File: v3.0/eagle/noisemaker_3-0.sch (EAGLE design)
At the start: 57 parts, among them IC1 REG1117

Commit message: board layout, all text complete. ready for manufacture, RC1
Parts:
- removed U$3: OSHW-LOGOS, SparkFun:OSHW-LOGOS
- added LOGO1: OSHW-LOGOM, SparkFun-Aesthetics:OSHW-LOGOM
- renumbered JP5 to ICSP, LED7 to LED1, LED8 to LED2, POWER to PWR
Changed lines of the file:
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@@
 <part name="JP7" library="SparkFun" deviceset="M12" device="PTH" value=""/>
 <part name="GND4" library="SparkFun" deviceset="GND" device=""/>
-<part name="U$3" library="SparkFun" deviceset="OSHW-LOGO" device="S"/>
 <part name="ATMEGA32U4" library="SparkFun-DigitalIC" deviceset="ATMEGA32U4" device="TQFP" value="ATMEGA32U4"/>
 <part name="XTAL" library="SparkFun" deviceset="CRYSTAL" device="5X3" value="16MHz"/>
@@
 <part name="GND8" library="SparkFun" deviceset="GND" device=""/>
 <part name="GND10" library="SparkFun" deviceset="GND" device=""/>
-<part name="POWER" library="adafruit" deviceset="LED" device="CHIPLED_1206" value="Red"/>
+<part name="PWR" library="adafruit" deviceset="LED" device="CHIPLED_1206" value="Red"/>
 <part name="R1" library="SparkFun-Passives" deviceset="RESISTOR" device="1206" value="1K"/>
 <part name="GND11" library="SparkFun" deviceset="GND" device=""/>
@@
 <part name="P+6" library="SparkFun" deviceset="3.3V" device="" value="VCC"/>
 <part name="P+7" library="SparkFun" deviceset="3.3V" device="" value="VCC"/>
-<part name="JP5" library="SparkFun" deviceset="AVR_SPI_PRG_6" device="PTH" value="AVR_SPI"/>
+<part name="ICSP" library="SparkFun" deviceset="AVR_SPI_PRG_6" device="PTH" value="AVR_SPI"/>
 <part name="GND1" library="SparkFun" deviceset="GND" device=""/>
 <part name="P+9" library="SparkFun" deviceset="3.3V" device="" value="VCC"/>
@@
 <part name="R13" library="SparkFun-Passives" deviceset="RESISTOR" device="1206" value="1k"/>
 <part name="GND19" library="SparkFun" deviceset="GND" device=""/>
-<part name="LED7" library="adafruit" deviceset="LED" device="3MM"/>
-<part name="LED8" library="adafruit" deviceset="LED" device="3MM"/>
+<part name="LED1" library="adafruit" deviceset="LED" device="3MM"/>
+<part name="LED2" library="adafruit" deviceset="LED" device="3MM"/>
 <part name="GND17" library="supply1" deviceset="GND" device=""/>
 <part name="R14" library="SparkFun-Passives" deviceset="RESISTOR" device="1206"/>
@@
 <part name="NEOPIXEL" library="SparkFun-Connectors" deviceset="M03" device="LONGPADS"/>
 <part name="P+8" library="SparkFun" deviceset="3.3V" device="" value="VCC"/>
+<part name="LOGO1" library="SparkFun-Aesthetics" deviceset="OSHW-LOGO" device="M" value="OSHW-LOGOM"/>
 </parts>
 <sheets>
@@
 <instance part="JP7" gate="G$1" x="60.96" y="101.6"/>
 <instance part="GND4" gate="1" x="139.7" y="109.22" rot="R270"/>
-<instance part="U$3" gate="G$1" x="243.84" y="175.26"/>
 <instance part="ATMEGA32U4" gate="G$1" x="180.34" y="121.92" smashed="yes">
 <attribute name="NAME" x="166.37" y="161.036" size="1.778" layer="95"/>
@@
 <instance part="GND8" gate="1" x="33.02" y="137.16"/>
 <instance part="GND10" gate="1" x="99.06" y="137.16"/>
-<instance part="POWER" gate="G$1" x="99.06" y="147.32"/>
+<instance part="PWR" gate="G$1" x="99.06" y="147.32"/>
 <instance part="R1" gate="G$1" x="99.06" y="154.94" rot="R90"/>
 <instance part="GND11" gate="1" x="76.2" y="137.16"/>
@@
 <attribute name="VALUE" x="297.942" y="91.186" size="1.778" layer="96" rot="R270"/>
 </instance>
-<instance part="JP5" gate="G$1" x="167.64" y="55.88"/>
+<instance part="ICSP" gate="G$1" x="167.64" y="55.88"/>
 <instance part="GND1" gate="1" x="180.34" y="48.26"/>
 <instance part="P+9" gate="G$1" x="180.34" y="60.96" smashed="yes">
@@
 <instance part="R13" gate="G$1" x="251.46" y="18.796"/>
 <instance part="GND19" gate="1" x="261.62" y="18.796" rot="R90"/>
-<instance part="LED7" gate="G$1" x="162.56" y="23.876" rot="R180"/>
-<instance part="LED8" gate="G$1" x="162.56" y="13.716" rot="R180"/>
+<instance part="LED1" gate="G$1" x="162.56" y="23.876" rot="R180"/>
+<instance part="LED2" gate="G$1" x="162.56" y="13.716" rot="R180"/>
 <instance part="GND17" gate="1" x="177.8" y="30.48" rot="R90"/>
 <instance part="R14" gate="G$1" x="167.64" y="9.652" rot="R180"/>
@@
 <attribute name="VALUE" x="105.918" y="86.614" size="1.778" layer="96" rot="R90"/>
 </instance>
+<instance part="LOGO1" gate="G$1" x="292.1" y="35.56"/>
 </instances>
 <busses>
@@
 <segment>
 <pinref part="GND10" gate="1" pin="GND"/>
-<pinref part="POWER" gate="G$1" pin="C"/>
+<pinref part="PWR" gate="G$1" pin="C"/>
 <wire x1="99.06" y1="142.24" x2="99.06" y2="139.7" width="0.1524" layer="91"/>
 </segment>
@@
 <wire x1="177.8" y1="53.34" x2="180.34" y2="53.34" width="0.1524" layer="91"/>
 <wire x1="180.34" y1="53.34" x2="180.34" y2="50.8" width="0.1524" layer="91"/>
-<pinref part="JP5" gate="G$1" pin="6"/>
+<pinref part="ICSP" gate="G$1" pin="6"/>
 <pinref part="GND1" gate="1" pin="GND"/>
 </segment>
@@
 <wire x1="160.02" y1="53.34" x2="147.32" y2="53.34" width="0.1524" layer="91"/>
 <label x="147.32" y="53.34" size="1.778" layer="95"/>
-<pinref part="JP5" gate="G$1" pin="5"/>
+<pinref part="ICSP" gate="G$1" pin="5"/>
 </segment>
 </net>
@@
 <wire x1="160.02" y1="55.88" x2="147.32" y2="55.88" width="0.1524" layer="91"/>
 <label x="147.32" y="55.88" size="1.778" layer="95"/>
-<pinref part="JP5" gate="G$1" pin="3"/>
+<pinref part="ICSP" gate="G$1" pin="3"/>
 </segment>
 </net>
@@
 <wire x1="160.02" y1="58.42" x2="147.32" y2="58.42" width="0.1524" layer="91"/>
 <label x="147.32" y="58.42" size="1.778" layer="95"/>
-<pinref part="JP5" gate="G$1" pin="1"/>
+<pinref part="ICSP" gate="G$1" pin="1"/>
 </segment>
 </net>
@@
 <wire x1="177.8" y1="55.88" x2="187.96" y2="55.88" width="0.1524" layer="91"/>
 <label x="182.88" y="55.88" size="1.778" layer="95"/>
-<pinref part="JP5" gate="G$1" pin="4"/>
+<pinref part="ICSP" gate="G$1" pin="4"/>
 </segment>
 </net>
@@
 <wire x1="177.8" y1="58.42" x2="180.34" y2="58.42" width="0.1524" layer="91"/>
 <wire x1="180.34" y1="60.96" x2="180.34" y2="58.42" width="0.1524" layer="91"/>
-<pinref part="JP5" gate="G$1" pin="2"/>
+<pinref part="ICSP" gate="G$1" pin="2"/>
 <pinref part="P+9" gate="G$1" pin="3.3V"/>
 </segment>
@@
 </segment>
 <segment>
-<pinref part="LED7" gate="G$1" pin="A"/>
-<pinref part="LED8" gate="G$1" pin="C"/>
+<pinref part="LED1" gate="G$1" pin="A"/>
+<pinref part="LED2" gate="G$1" pin="C"/>
 <wire x1="162.56" y1="18.796" x2="162.56" y2="20.32" width="0.1524" layer="91"/>
 <wire x1="162.56" y1="20.32" x2="162.56" y2="21.336" width="0.1524" layer="91"/>
@@
 <net name="N$10" class="0">
 <segment>
-<pinref part="POWER" gate="G$1" pin="A"/>
+<pinref part="PWR" gate="G$1" pin="A"/>
 <pinref part="R1" gate="G$1" pin="1"/>
 </segment>
@@
 <segment>
 <pinref part="R18" gate="G$1" pin="1"/>
-<pinref part="LED7" gate="G$1" pin="C"/>
+<pinref part="LED1" gate="G$1" pin="C"/>
 <wire x1="162.56" y1="30.48" x2="162.56" y2="28.956" width="0.1524" layer="91"/>
 </segment>
@@
 <net name="N$13" class="0">
 <segment>
-<pinref part="LED8" gate="G$1" pin="A"/>
+<pinref part="LED2" gate="G$1" pin="A"/>
 <wire x1="162.56" y1="11.176" x2="162.56" y2="9.652" width="0.1524" layer="91"/>
 <pinref part="R14" gate="G$1" pin="2"/>

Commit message: small adjustments, this is final board
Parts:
- R14, R18: value (none) -> 330
- R15, R19: value (none) -> 10k
- R3, R8: value (none) -> 1M
- R9: value (none) -> 22k
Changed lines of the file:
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@@
 <part name="C11" library="SparkFun-Capacitors" deviceset="CAP" device="1206" value="0.1uF"/>
 <part name="P+5" library="SparkFun" deviceset="3.3V" device="" value="VCC"/>
-<part name="R3" library="SparkFun-Passives" deviceset="RESISTOR" device="1206"/>
-<part name="R8" library="SparkFun-Passives" deviceset="RESISTOR" device="1206"/>
-<part name="R9" library="SparkFun-Passives" deviceset="RESISTOR" device="1206"/>
+<part name="R3" library="SparkFun-Passives" deviceset="RESISTOR" device="1206" value="1M"/>
+<part name="R8" library="SparkFun-Passives" deviceset="RESISTOR" device="1206" value="1M"/>
+<part name="R9" library="SparkFun-Passives" deviceset="RESISTOR" device="1206" value="22k"/>
 <part name="NPN" library="SparkFun-DiscreteSemi" deviceset="TRANSISTOR_NPN" device="SOT23-3"/>
 <part name="GND16" library="supply1" deviceset="GND" device=""/>
@@
 <part name="JP4" library="SparkFun-Connectors" deviceset="M01" device="PTH"/>
 <part name="SENSOR1" library="photo-elements" deviceset="M9960_11" device="" technology="B"/>
-<part name="R15" library="SparkFun-Passives" deviceset="RESISTOR" device="1206"/>
-<part name="R19" library="SparkFun-Passives" deviceset="RESISTOR" device="1206"/>
+<part name="R15" library="SparkFun-Passives" deviceset="RESISTOR" device="1206" value="10k"/>
+<part name="R19" library="SparkFun-Passives" deviceset="RESISTOR" device="1206" value="10k"/>
 <part name="SENSOR2" library="photo-elements" deviceset="M9960_11" device="" technology="B"/>
 <part name="GND21" library="supply1" deviceset="GND" device=""/>
@@
 <part name="LED2" library="adafruit" deviceset="LED" device="3MM"/>
 <part name="GND17" library="supply1" deviceset="GND" device=""/>
-<part name="R14" library="SparkFun-Passives" deviceset="RESISTOR" device="1206"/>
-<part name="R18" library="SparkFun-Passives" deviceset="RESISTOR" device="1206"/>
+<part name="R14" library="SparkFun-Passives" deviceset="RESISTOR" device="1206" value="330"/>
+<part name="R18" library="SparkFun-Passives" deviceset="RESISTOR" device="1206" value="330"/>
 <part name="POLE3" library="SparkFun-Connectors" deviceset="M01" device="PTH_LONGPAD"/>
 <part name="P+13" library="SparkFun" deviceset="3.3V" device="" value="VCC"/>

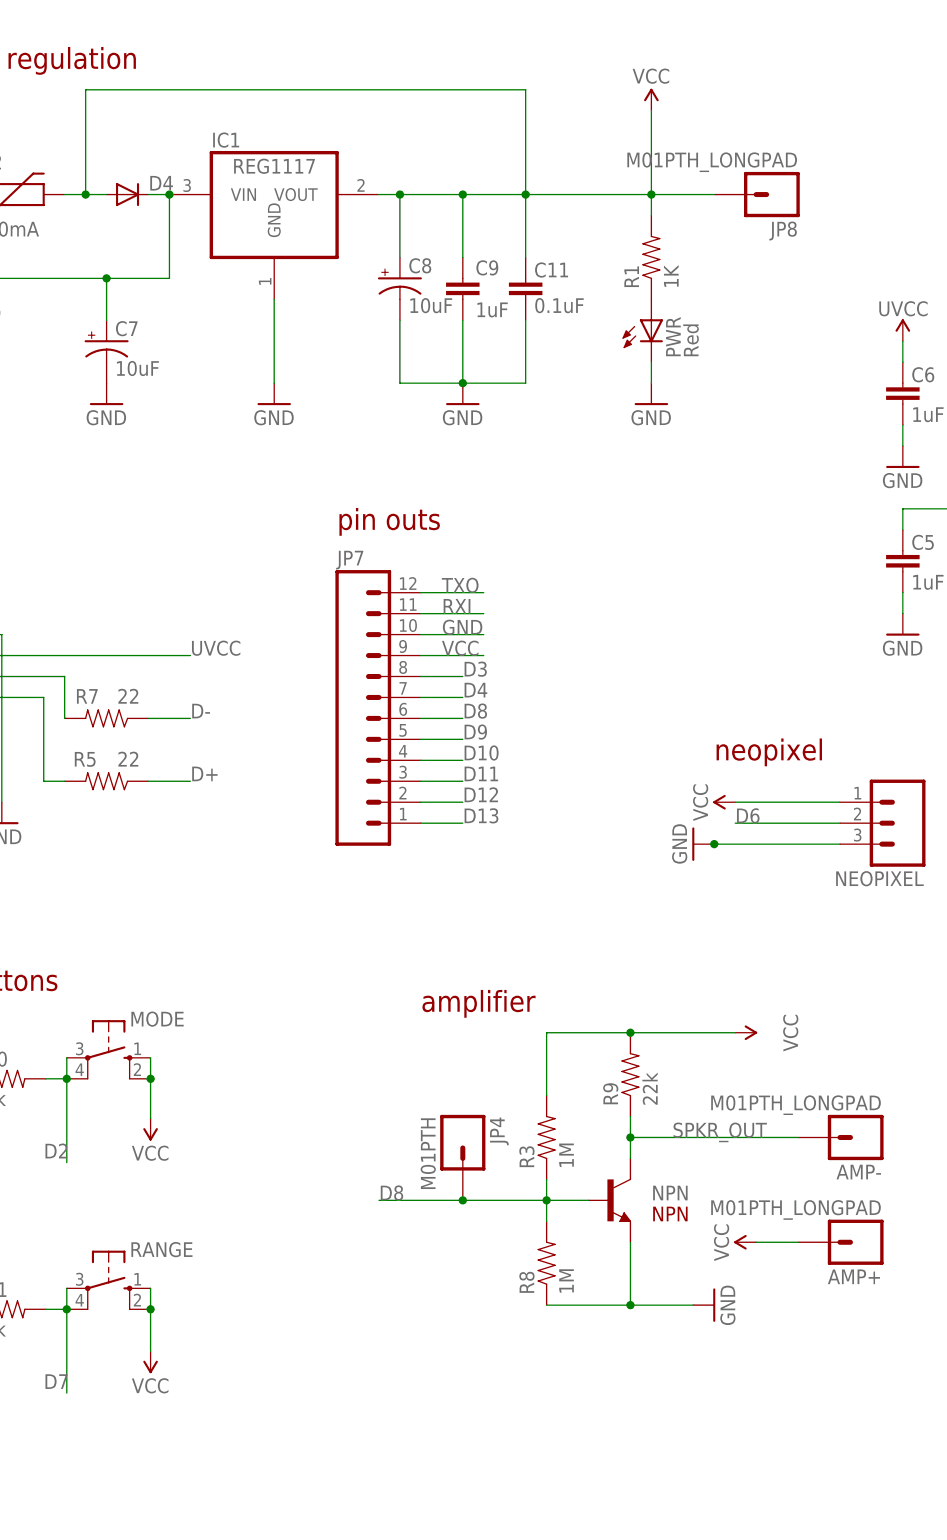
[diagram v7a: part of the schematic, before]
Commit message: updated voltage regulator, added second footprint for NPN options
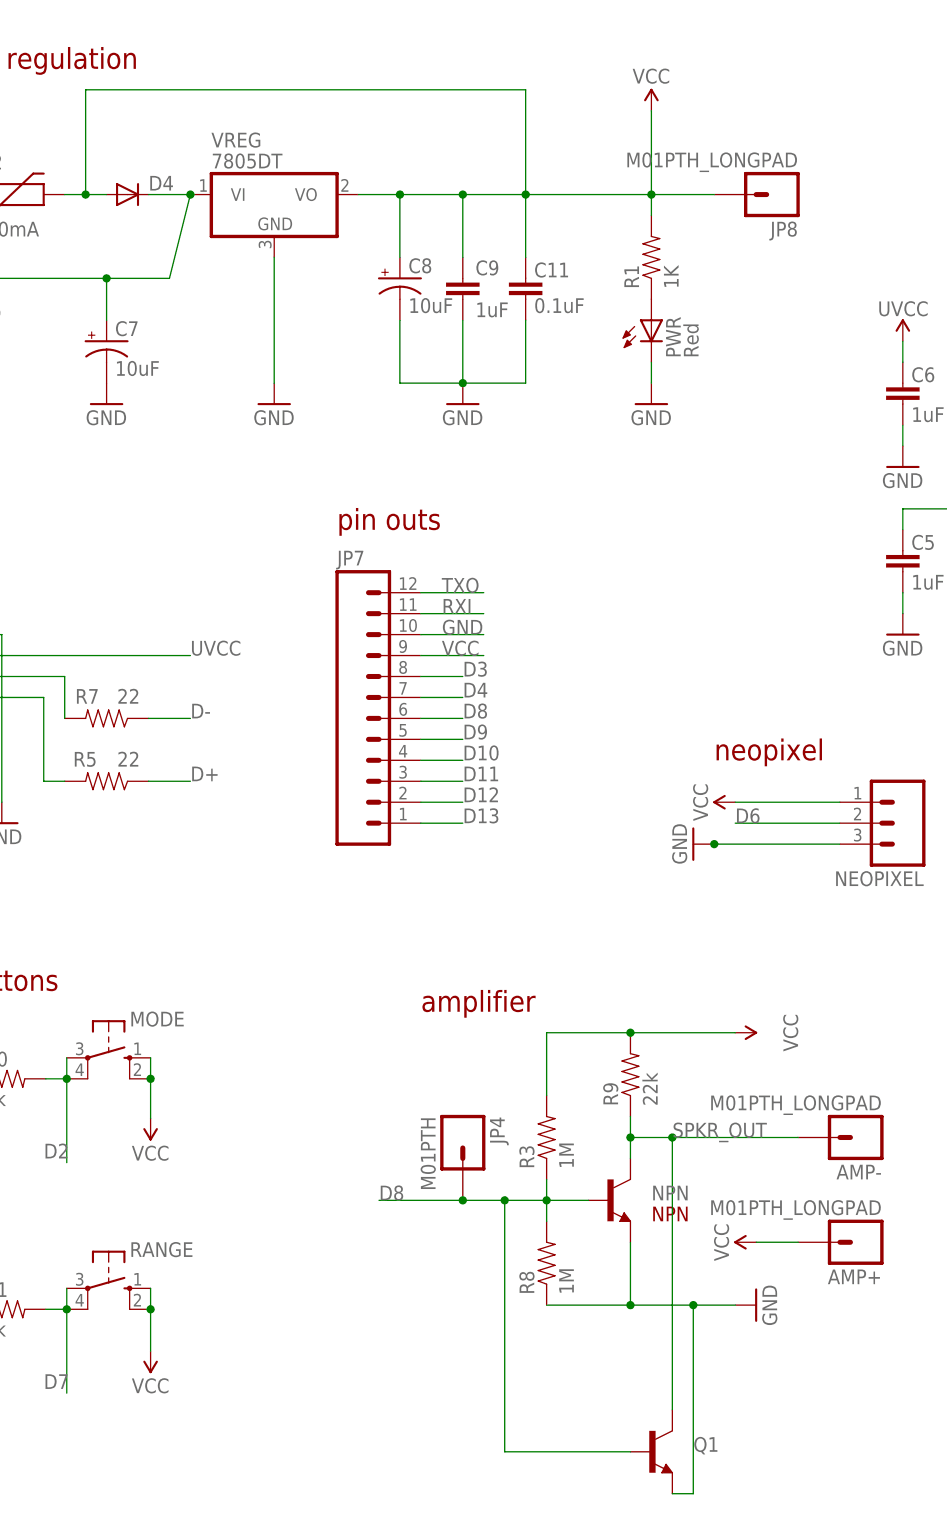
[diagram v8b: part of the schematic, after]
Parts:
- removed IC1: REG1117, burr-brown:REG1117
- added Q1: (no value), SparkFun-DiscreteSemi:TRANSISTOR_NPNTO-92-AMMO
- added VREG: 7805DT, linear:7805DT
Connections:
- net D8: now also Q1.B
- net GND: now also Q1.E, VREG.GND; no longer IC1.GND
- net RAW: now also VREG.VI; no longer IC1.VIN
- net SPKR_OUT: now also Q1.C
- net VCC: now also VREG.VO; no longer IC1.VOUT
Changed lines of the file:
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@@
 <part name="JP3" library="SparkFun-Connectors" deviceset="USB" device="PTH" value="USB-B"/>
 <part name="GND5" library="SparkFun" deviceset="GND" device=""/>
-<part name="IC1" library="burr-brown" deviceset="REG1117" device=""/>
 <part name="GND3" library="SparkFun" deviceset="GND" device=""/>
 <part name="F2" library="SparkFun" deviceset="PTC" device="SMD" value="500mA"/>
@@
 <part name="P+8" library="SparkFun" deviceset="3.3V" device="" value="VCC"/>
 <part name="LOGO1" library="SparkFun-Aesthetics" deviceset="OSHW-LOGO" device="M" value="OSHW-LOGOM"/>
+<part name="Q1" library="SparkFun-DiscreteSemi" deviceset="TRANSISTOR_NPN" device="TO-92-AMMO"/>
+<part name="VREG" library="linear" deviceset="78*" device="DT" technology="05"/>
 </parts>
 <sheets>
@@
 <instance part="JP3" gate="G$1" x="12.7" y="109.22" rot="R180"/>
 <instance part="GND5" gate="1" x="20.32" y="86.36"/>
-<instance part="IC1" gate="G$1" x="53.34" y="162.56"/>
 <instance part="GND3" gate="1" x="53.34" y="137.16"/>
 <instance part="F2" gate="G$1" x="20.32" y="162.56"/>
@@
 <instance part="R9" gate="G$1" x="96.52" y="55.88" rot="R90"/>
 <instance part="NPN" gate="G$1" x="93.98" y="40.64"/>
-<instance part="GND16" gate="1" x="106.68" y="27.94" rot="R90"/>
+<instance part="GND16" gate="1" x="111.76" y="27.94" rot="R90"/>
 <instance part="AMP-" gate="G$1" x="124.46" y="48.26" rot="R180"/>
 <instance part="AMP+" gate="G$1" x="124.46" y="35.56" rot="R180"/>
@@
 </instance>
 <instance part="LOGO1" gate="G$1" x="292.1" y="35.56"/>
+<instance part="Q1" gate="G$1" x="99.06" y="10.16"/>
+<instance part="VREG" gate="A1" x="53.34" y="162.56"/>
 </instances>
 <busses>
@@
 </segment>
 <segment>
-<pinref part="IC1" gate="G$1" pin="GND"/>
 <pinref part="GND3" gate="1" pin="GND"/>
-<wire x1="53.34" y1="139.7" x2="53.34" y2="149.86" width="0.1524" layer="91"/>
+<wire x1="53.34" y1="139.7" x2="53.34" y2="154.94" width="0.1524" layer="91"/>
+<pinref part="VREG" gate="A1" pin="GND"/>
 </segment>
 <segment>
@@
 <junction x="96.52" y="27.94"/>
 <pinref part="GND16" gate="1" pin="GND"/>
+<wire x1="109.22" y1="27.94" x2="104.14" y2="27.94" width="0.1524" layer="91"/>
+<wire x1="104.14" y1="27.94" x2="104.14" y2="5.08" width="0.1524" layer="91"/>
+<pinref part="Q1" gate="G$1" pin="E"/>
+<wire x1="104.14" y1="5.08" x2="101.6" y2="5.08" width="0.1524" layer="91"/>
+<junction x="104.14" y="27.94"/>
 </segment>
 <segment>
@@
 </segment>
 <segment>
-<pinref part="IC1" gate="G$1" pin="VOUT"/>
-<wire x1="66.04" y1="162.56" x2="68.58" y2="162.56" width="0.1524" layer="91"/>
+<wire x1="63.5" y1="162.56" x2="68.58" y2="162.56" width="0.1524" layer="91"/>
 <wire x1="68.58" y1="162.56" x2="76.2" y2="162.56" width="0.1524" layer="91"/>
 <wire x1="76.2" y1="162.56" x2="83.82" y2="162.56" width="0.1524" layer="91"/>
@@
 <pinref part="JP8" gate="G$1" pin="1"/>
 <wire x1="106.68" y1="162.56" x2="99.06" y2="162.56" width="0.1524" layer="91"/>
+<pinref part="VREG" gate="A1" pin="VO"/>
 </segment>
 <segment>
@@
 <net name="RAW" class="1">
 <segment>
-<pinref part="IC1" gate="G$1" pin="VIN"/>
 <pinref part="D4" gate="G$1" pin="C"/>
-<wire x1="40.64" y1="162.56" x2="38.1" y2="162.56" width="0.1524" layer="91"/>
+<wire x1="43.18" y1="162.56" x2="38.1" y2="162.56" width="0.1524" layer="91"/>
 <wire x1="7.62" y1="152.4" x2="33.02" y2="152.4" width="0.1524" layer="91"/>
 <wire x1="33.02" y1="152.4" x2="40.64" y2="152.4" width="0.1524" layer="91"/>
-<wire x1="40.64" y1="152.4" x2="40.64" y2="162.56" width="0.1524" layer="91"/>
-<junction x="40.64" y="162.56"/>
+<wire x1="40.64" y1="152.4" x2="43.18" y2="162.56" width="0.1524" layer="91"/>
 <label x="7.62" y="152.4" size="1.778" layer="95"/>
 <pinref part="C7" gate="G$1" pin="+"/>
 <wire x1="33.02" y1="147.32" x2="33.02" y2="152.4" width="0.1524" layer="91"/>
 <junction x="33.02" y="152.4"/>
+<pinref part="VREG" gate="A1" pin="VI"/>
+<junction x="43.18" y="162.56"/>
 </segment>
 <segment>
@@
 <wire x1="91.44" y1="40.64" x2="86.36" y2="40.64" width="0.1524" layer="91"/>
 <junction x="86.36" y="40.64"/>
-<wire x1="86.36" y1="40.64" x2="76.2" y2="40.64" width="0.1524" layer="91"/>
+<wire x1="86.36" y1="40.64" x2="81.28" y2="40.64" width="0.1524" layer="91"/>
 <label x="66.04" y="40.64" size="1.778" layer="95"/>
 <pinref part="JP4" gate="G$1" pin="1"/>
+<wire x1="81.28" y1="40.64" x2="76.2" y2="40.64" width="0.1524" layer="91"/>
 <wire x1="76.2" y1="40.64" x2="66.04" y2="40.64" width="0.1524" layer="91"/>
 <junction x="76.2" y="40.64"/>
+<wire x1="81.28" y1="40.64" x2="81.28" y2="10.16" width="0.1524" layer="91"/>
+<junction x="81.28" y="40.64"/>
+<pinref part="Q1" gate="G$1" pin="B"/>
+<wire x1="81.28" y1="10.16" x2="96.52" y2="10.16" width="0.1524" layer="91"/>
 </segment>
 <segment>
@@
 <wire x1="96.52" y1="45.72" x2="96.52" y2="48.26" width="0.1524" layer="91"/>
 <wire x1="96.52" y1="48.26" x2="96.52" y2="50.8" width="0.1524" layer="91"/>
-<wire x1="96.52" y1="48.26" x2="116.84" y2="48.26" width="0.1524" layer="91"/>
+<wire x1="96.52" y1="48.26" x2="101.6" y2="48.26" width="0.1524" layer="91"/>
 <junction x="96.52" y="48.26"/>
 <label x="101.6" y="48.26" size="1.778" layer="95"/>
 <pinref part="AMP-" gate="G$1" pin="1"/>
-</segment>
-</net>
+<pinref part="Q1" gate="G$1" pin="C"/>
+<wire x1="101.6" y1="48.26" x2="116.84" y2="48.26" width="0.1524" layer="91"/>
+<wire x1="101.6" y1="15.24" x2="101.6" y2="48.26" width="0.1524" layer="91"/>
+<junction x="101.6" y="48.26"/>
+</segment>
+</net>
